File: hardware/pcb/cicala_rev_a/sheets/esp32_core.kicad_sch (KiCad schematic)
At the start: 35 parts, among them J4 TC2030 recovery pads, SW1 CATEGORY KSC321GLFS, SW2 NEXT KSC321GLFS, U1 ESP32-S3-WROOM-1-N16 / WROOM-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

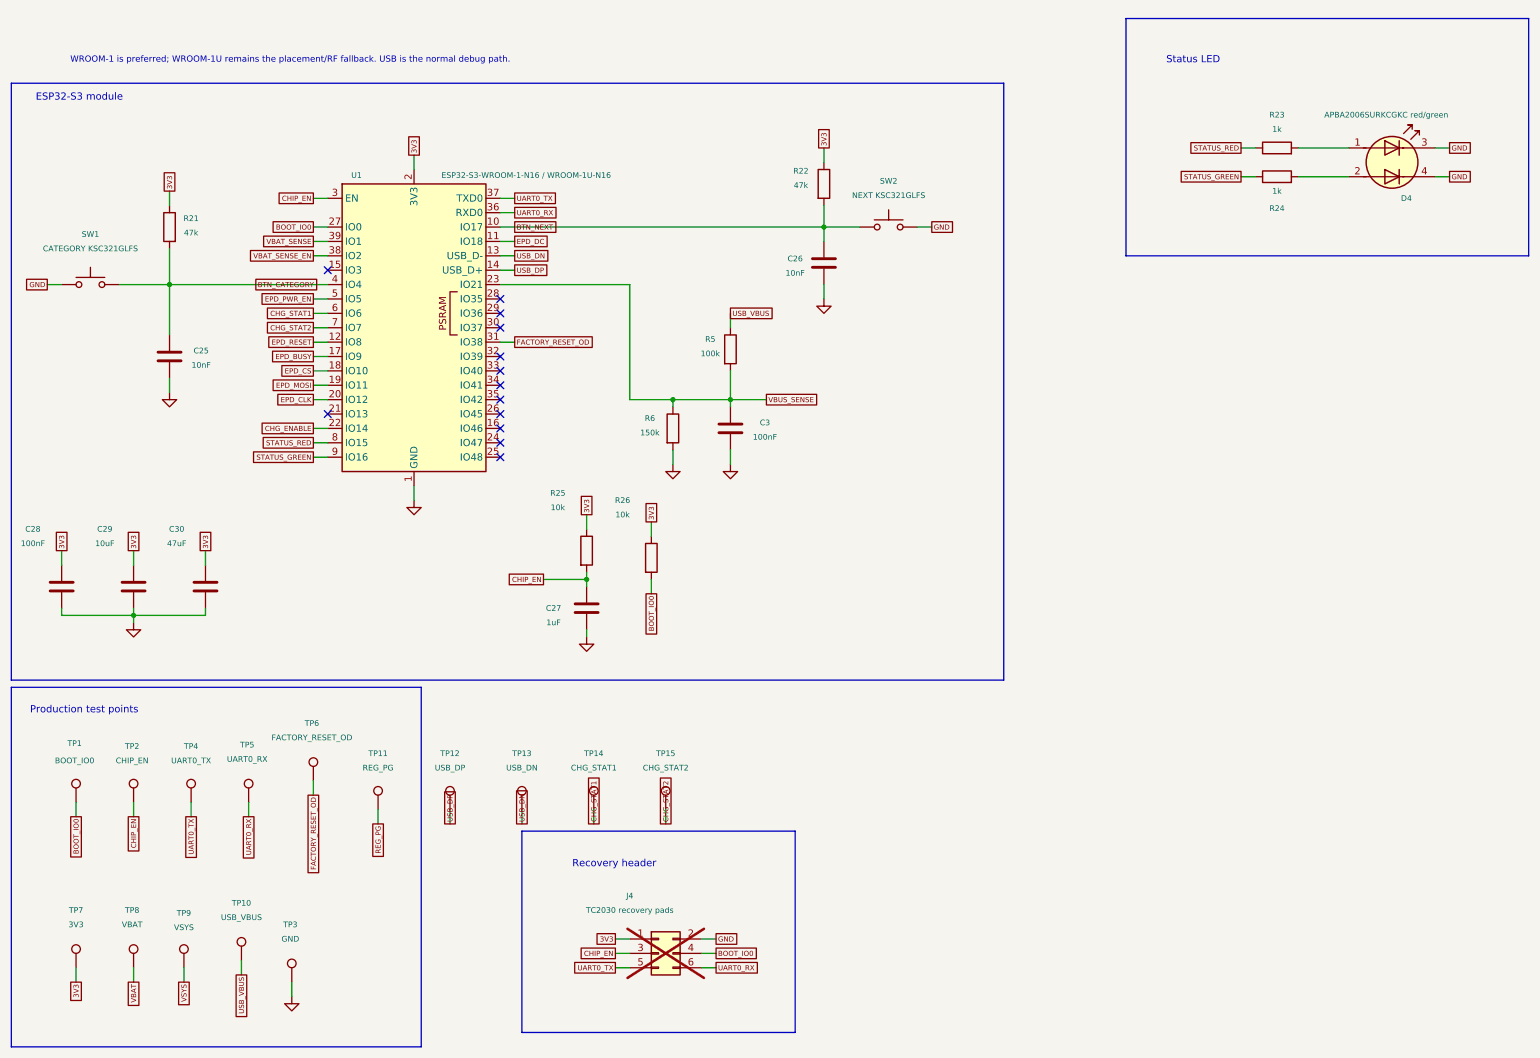
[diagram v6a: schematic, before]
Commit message: refactor(hw): make the root sheet a real hierarchy
The root was three boxes and a filename; every cross-sheet signal travelled
by global label, so nothing recorded which block produced a signal and which
consumed it. The 19 nets that actually cross a sheet boundary are now
hierarchical: each child carries a directional hierarchical label and the
root carries the matching sheet pin, wired block to block. The root also
states the power flow in words.

GND stays global; a ground symbol reads better than a pin on every block.
Root-level global labels keep the plain net names that pin_contract.csv and
the firmware refer to, rather than the sheet-path names a local label gives.

Connectivity is unchanged: the exported netlist is identical to the one
before the conversion, net for net and pin for pin.

Also hides the PWR_FLAG references, moves the USB shield network and the
cell-current link inside the blocks they belong to, and gives every page the
same company, revision and date.

Co-Authored-By: Claude Opus 5 <noreply@anthropic.com>
Claude-Session: https://claude.ai/code/session_01E5vy1HJsPztSk9nFw6j5Ko
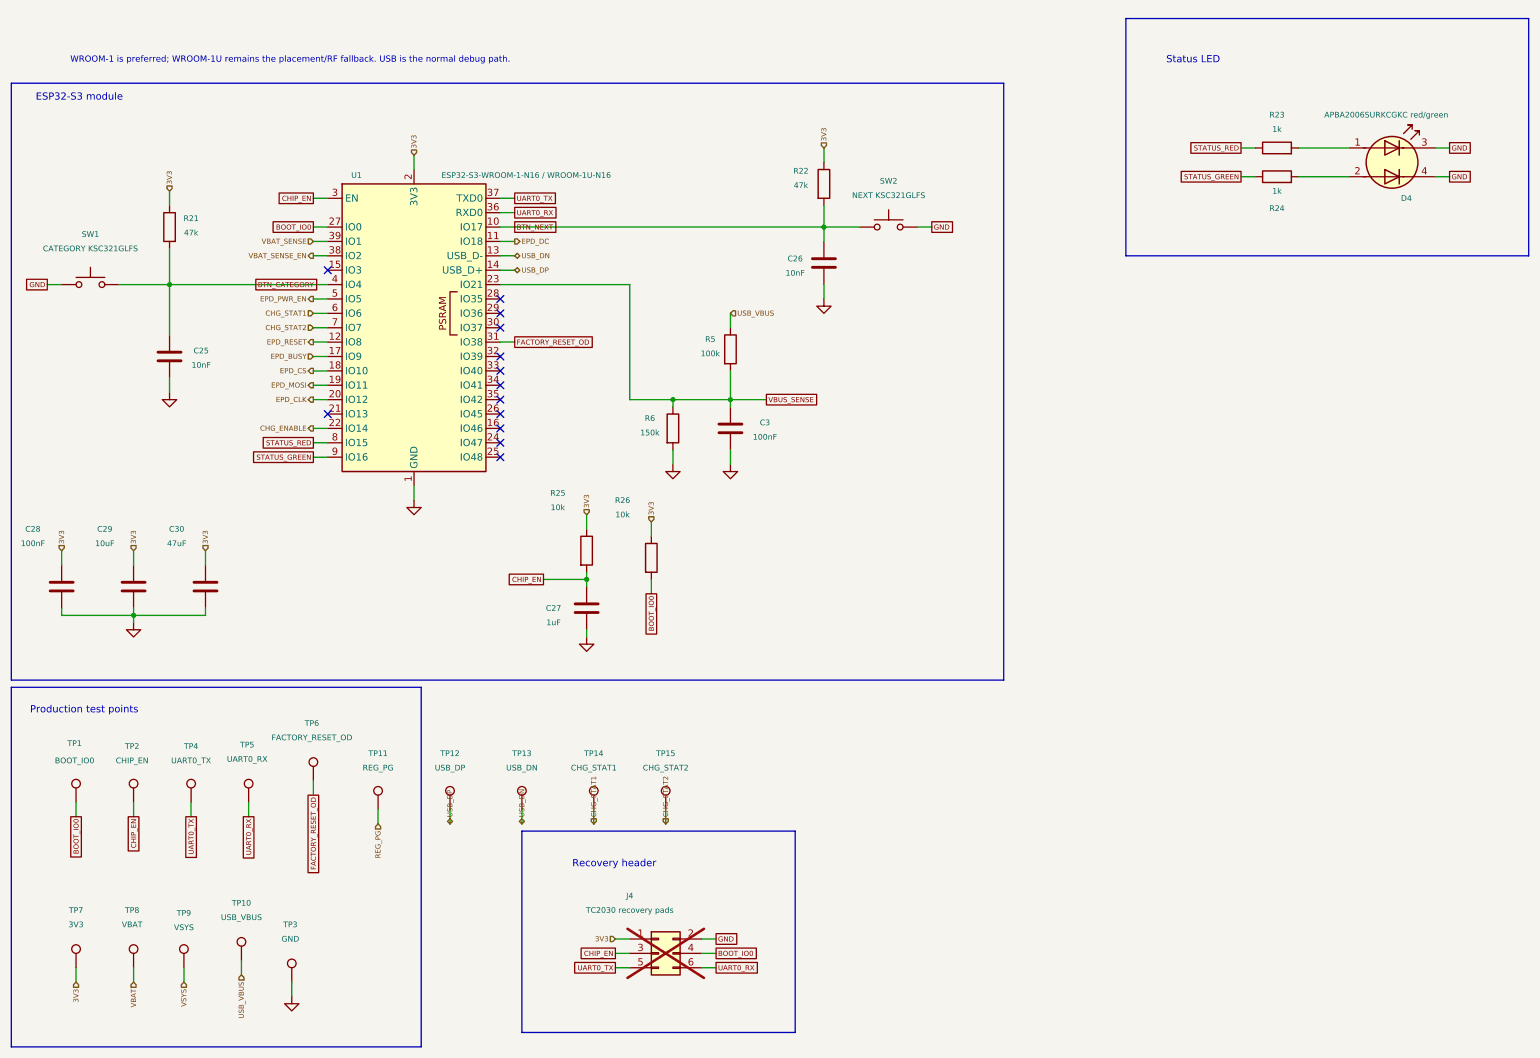
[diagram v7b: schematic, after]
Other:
- company: (none) -> Cicala
